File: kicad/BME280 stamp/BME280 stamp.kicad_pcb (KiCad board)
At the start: 4 copper layers, 15.2 x 15.2 mm, 5 parts, among them U1 BME280

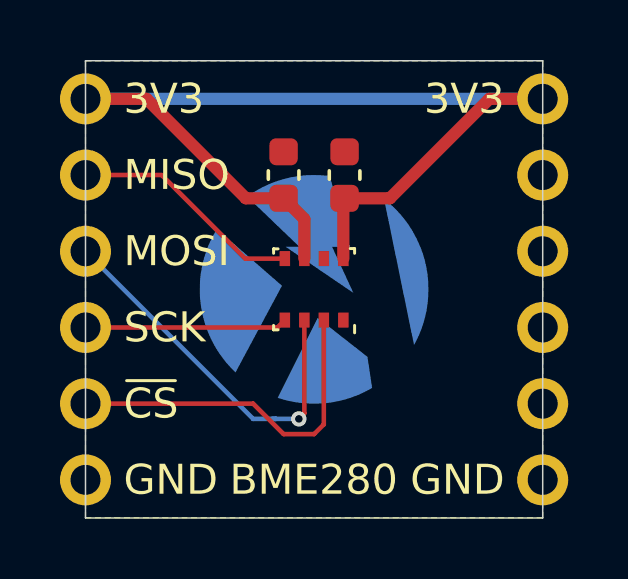
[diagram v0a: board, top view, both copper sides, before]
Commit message: Added labels to BME280 stamp
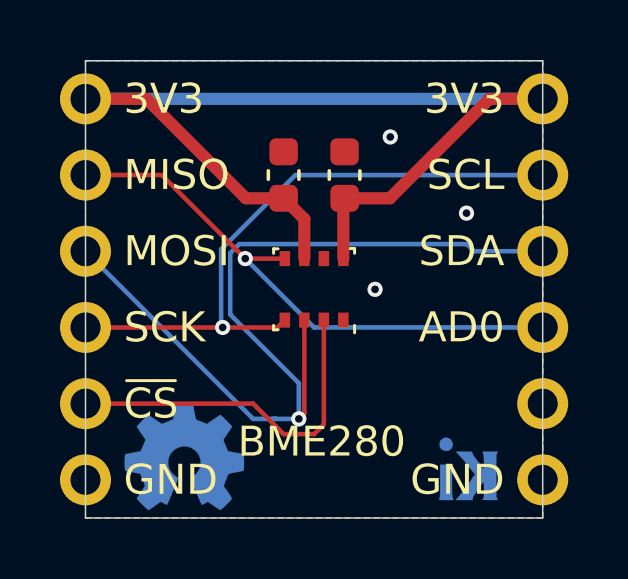
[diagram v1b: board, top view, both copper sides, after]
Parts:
- added G2: Designed with, KwanSystems:Symbol_KiCAD-Logo_CopperAndSilkScreenTop_small, B.Cu at (112.5, 115.3)
- added G3: OSHW, KwanSystems:OSHW-Symbol_4x3.6mm_SolderMask, B.Cu at (104.9, 114.8)
- G1: value KwanSystems -> github.com/kwan3217; footprint KwanSystems:StKwansSoldermask -> KwanSystems:KWAN_CIRCLE
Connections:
- J101 pad 10: (no net) -> /MOSI
- J101 pad 11: unconnected-(J101-SCL-Pad11) -> /SCK
- J101 pad 9: unconnected-(J101-X1-Pad9) -> /MISO
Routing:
- net /MOSI: track 13.3 -> 30.4 mm
- net /SCK: track 6.75 -> 21.1 mm, vias 0 -> 1
- net /MISO: track 7.80 -> 18.7 mm, vias 0 -> 1
- net GND: vias 0 -> 3
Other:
- board text added: "2023-04-01"
- board text added: "23.04"

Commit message: As ordered on 03 Apr 2023. Some but not all numbers-on-hand have been updated.
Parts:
- renumbered C1 to C506, C106 to C508, J101 to J501, U1 to U501
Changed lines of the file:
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@@
     (property "ki_keywords" "capacitor cap")
     (attr smd)
-    (fp_text reference "C106" (at 0 -1.43 90) (layer "F.SilkS") hide
+    (fp_text reference "C508" (at 0 -1.43 90) (layer "F.SilkS") hide
         (effects (font (size 1 1) (thickness 0.15)))
     )
@@
     (property "Sheetname" "")
     (attr smd)
-    (fp_text reference "J101" (at 0 -0.5 unlocked) (layer "F.SilkS") hide
+    (fp_text reference "J501" (at 0 -0.5 unlocked) (layer "F.SilkS") hide
         (effects (font (size 1 1) (thickness 0.1)))
     )
@@
     (property "ki_keywords" "Bosch pressure humidity temperature environment environmental measurement digital")
     (attr smd)
-    (fp_text reference "U1" (at 0.015 -2.465) (layer "F.SilkS") hide
+    (fp_text reference "U501" (at 0.015 -2.465) (layer "F.SilkS") hide
         (effects (font (size 1 1) (thickness 0.15)))
     )
@@
     (property "ki_keywords" "capacitor cap")
     (attr smd)
-    (fp_text reference "C1" (at 0 -1.43 90) (layer "F.SilkS") hide
-        (effects (font (size 1 1) (thickness 0.15)))
-    )
+    (fp_text reference "C506" (at 0 -1.43 90) (layer "F.SilkS") hide
+        (effects (font (size 1 1) (thickness 0.15)))
+    )
